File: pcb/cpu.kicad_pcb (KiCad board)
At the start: 2 copper layers, 181.5 x 172.5 mm, 173 parts, among them J1 Conn_01x05, J2 Conn_02x20_Odd_Even, J3 Conn_01x03, SW1 SW_DIP_x03 - Clock Source Sel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, SW2 SW_Push, SW4 SW_Push, U1 LM555, U10 74HCT574, U11 74HC245, U112 74LS574, U113 SST39SF040, U114 74HC04, U117 74LS08, U119 74LS32, U12 74HCT574, U120 74LS32, U121 74HCT574, U122 74HC245, U13 74LS273, U14 74HCT574, U15 74LS273, U16 74HCT574, U17 74HC238, U18 74HCT574, U19 74HC238, U2 74HC14, U20 74HC238, U21 74HCT574, U22 74HCT574, U23 74LS139, U24 28C256, U25 HDSP-7803, U26 HDSP-7803, U27 HDSP-7803, U28 HDSP-7803, U29 74HCT574, U3 74151, U30 74HC86, U31 SST39SF040, U32 74HCT574, U33 74LS08, U34 74HCT574, U35 74LS107, U36 74HC238, U37 74LS138, U38 74HC74, U39 74HC590, U4 LM555 - Button Clock, U40 74HCT574, U41 74LS138, U49 74HCT574, U5 74HC04, U50 74HCT574, U6 74HC590, U7 74HC245, U71 SST39SF040, U72 628128, U8 74HCT574, U80 74HCT574, U81 74HCT574, U82 74HCT574, U83 74HC245, U84 628128, U85 74LS153, U86 74HC245, U87 74LS574, U88 SST39SF040, U89 74LS574, U9 74HC245, U90 SST39SF040, U95 74LS154, U96 74LS154, Y1 12MHz

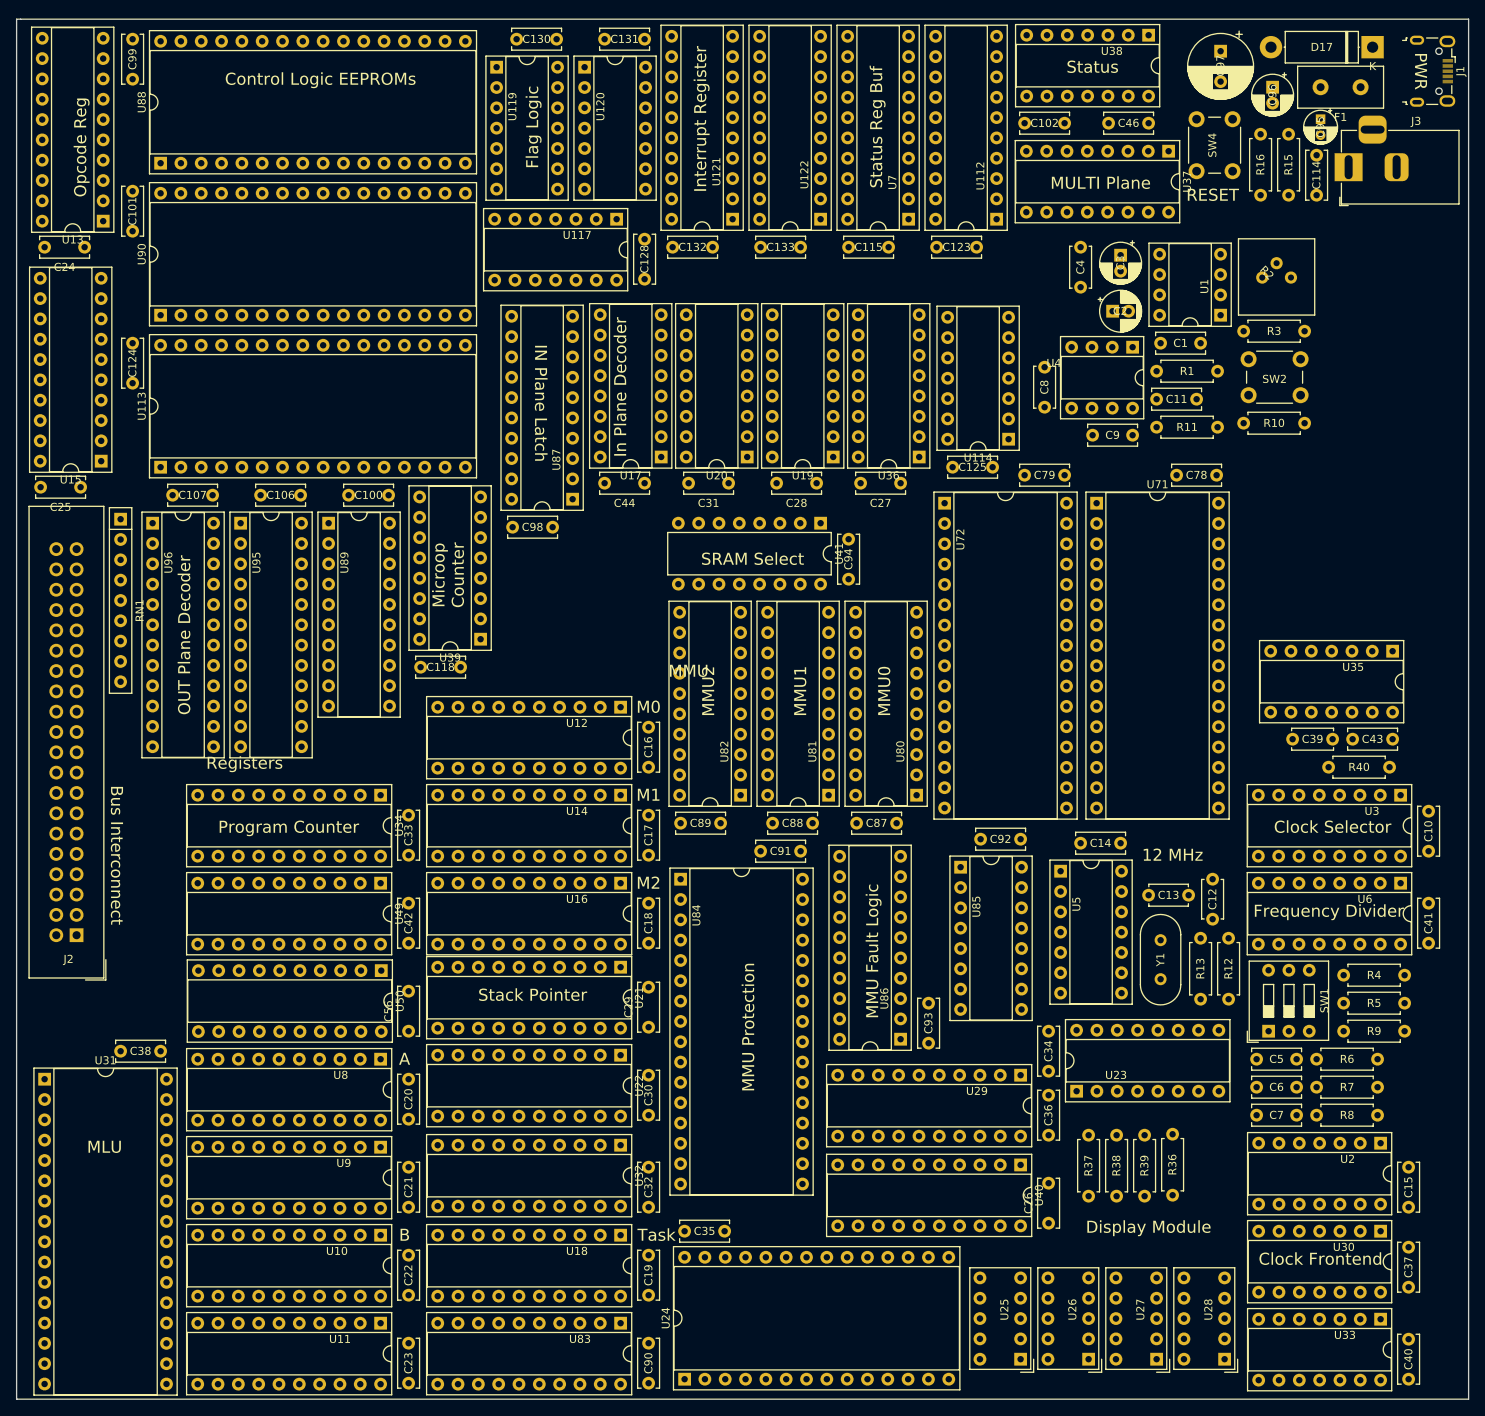
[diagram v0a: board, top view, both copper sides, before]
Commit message: Work on moving everything to 32 bit + proper paging + memory mapped IO.
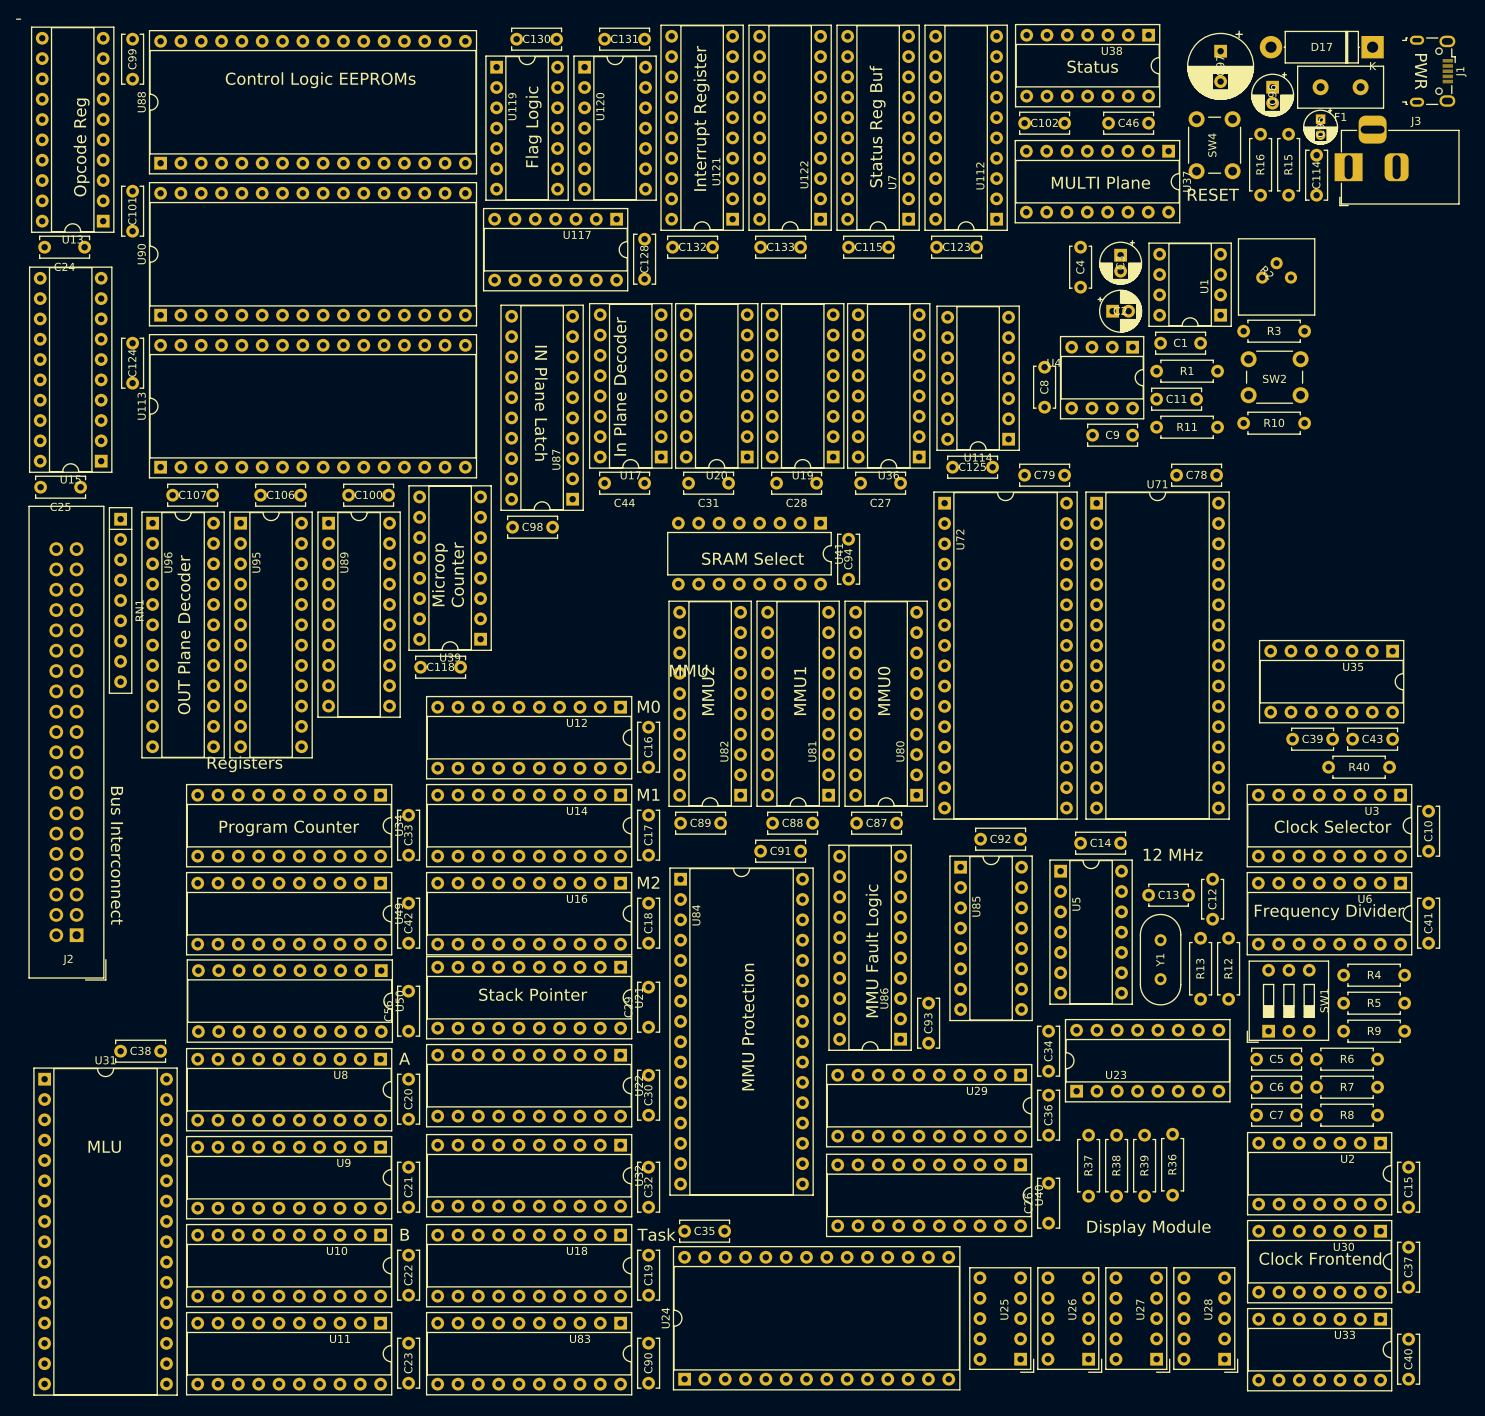
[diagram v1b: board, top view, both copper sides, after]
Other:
- board outline removed
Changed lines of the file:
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@@
-(kicad_pcb (version 20171130) (host pcbnew "(6.0.0-rc1-dev-290-g3eb3db02c)")
+(kicad_pcb (version 20171130) (host pcbnew 5.0.0-fee4fd1~66~ubuntu18.04.1)
   (general
     (thickness 1.6)
-    (drawings 41)
+    (drawings 37)
     (tracks 0)
     (zones 0)
@@
     (zone_45_only no)
     (trace_min 0.2)
+    (segment_width 0.2)
+    (edge_width 0.15)
     (via_size 0.6)
     (via_drill 0.3)
@@
     (uvia_min_size 0.2)
     (uvia_min_drill 0.1)
-    (edge_width 0.15)
-    (segment_width 0.2)
     (pcb_text_width 0.3)
     (pcb_text_size 1.5 1.5)
@@
   )
   (gr_line (start -0.5 0) (end 0 0) (layer Edge.Cuts) (width 0.15))
-  (gr_line (start -0.5 172.5) (end -0.5 0) (layer Edge.Cuts) (width 0.15))
-  (gr_line (start 181 172.5) (end -0.5 172.5) (layer Edge.Cuts) (width 0.15))
-  (gr_line (start 181 0) (end 181 172.5) (layer Edge.Cuts) (width 0.15))
-  (gr_line (start 0 0) (end 181 0) (layer Edge.Cuts) (width 0.15))
   (gr_text "MMU Fault Logic" (at 106.5 116.5 90) (layer F.SilkS)
     (effects (font (size 1.5 1.5) (thickness 0.3)))

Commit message: Conversion to 32-bit word mostly done?
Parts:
- removed C115, C128, C130, C131, C133: 0.1uF, Capacitor_THT:C_Disc_D6.0mm_W2.5mm_P5.00mm
- removed R36, R37, R38, R39: 100, Resistor_THT:R_Axial_DIN0207_L6.3mm_D2.5mm_P7.62mm_Horizontal
- removed U117: 74LS08, Package_DIP:DIP-14_W7.62mm_Socket
- removed U119, U120: 74LS32, Package_DIP:DIP-14_W7.62mm_Socket
- removed U122, U86: 74HC245, Package_DIP:DIP-20_W7.62mm_Socket
- added C45: 0.1uF, Capacitor_THT:C_Disc_D6.0mm_W2.5mm_P5.00mm, F.Cu at (354.9, 39.0)
- added C47: 0.1uF, Capacitor_THT:C_Disc_D6.0mm_W2.5mm_P5.00mm, F.Cu at (354.9, 35.0)
- added C48: 0.1uF, Capacitor_THT:C_Disc_D6.0mm_W2.5mm_P5.00mm, F.Cu at (354.9, 43.1)
- added C49: 0.1uF, Capacitor_THT:C_Disc_D6.0mm_W2.5mm_P5.00mm, F.Cu at (401.9, 7.88)
- added C50: 0.1uF, Capacitor_THT:C_Disc_D6.0mm_W2.5mm_P5.00mm, F.Cu at (410.1, 7.88)
- added C51: 0.1uF, Capacitor_THT:C_Disc_D6.0mm_W2.5mm_P5.00mm, F.Cu at (401.9, 11.9)
- added C52: 0.1uF, Capacitor_THT:C_Disc_D6.0mm_W2.5mm_P5.00mm, F.Cu at (410.1, 11.9)
- added C53: 0.1uF, Capacitor_THT:C_Disc_D6.0mm_W2.5mm_P5.00mm, F.Cu at (401.9, 16.0)
- added C54: 0.1uF, Capacitor_THT:C_Disc_D6.0mm_W2.5mm_P5.00mm, F.Cu at (401.9, 20.0)
- added C55: 0.1uF, Capacitor_THT:C_Disc_D6.0mm_W2.5mm_P5.00mm, F.Cu at (390.2, 27.4)
- added C57: 0.1uF, Capacitor_THT:C_Disc_D6.0mm_W2.5mm_P5.00mm, F.Cu at (406.5, 118.1)
- added C58: 0.1uF, Capacitor_THT:C_Disc_D6.0mm_W2.5mm_P5.00mm, F.Cu at (398.3, 118.1)
- added C59: 0.1uF, Capacitor_THT:C_Disc_D6.0mm_W2.5mm_P5.00mm, F.Cu at (410.1, 89.7)
- added C60: 0.1uF, Capacitor_THT:C_Disc_D6.0mm_W2.5mm_P5.00mm, F.Cu at (418.2, 85.6)
- added C61: 0.1uF, Capacitor_THT:C_Disc_D6.0mm_W2.5mm_P5.00mm, F.Cu at (410.1, 85.6)
- added C62: 0.1uF, Capacitor_THT:C_Disc_D6.0mm_W2.5mm_P5.00mm, F.Cu at (362.9, 76.8)
- added C63: 0.1uF, Capacitor_THT:C_Disc_D6.0mm_W2.5mm_P5.00mm, F.Cu at (354.7, 76.8)
- added C64: 0.1uF, Capacitor_THT:C_Disc_D6.0mm_W2.5mm_P5.00mm, F.Cu at (354.7, 80.9)
- added C65: 0.1uF, Capacitor_THT:C_Disc_D6.0mm_W2.5mm_P5.00mm, F.Cu at (468.4, 7.88)
- added C66: 0.1uF, Capacitor_THT:C_Disc_D6.0mm_W2.5mm_P5.00mm, F.Cu at (476.5, 7.88)
- added C67: 0.1uF, Capacitor_THT:C_Disc_D6.0mm_W2.5mm_P5.00mm, F.Cu at (468.4, 11.9)
- added C68: 0.1uF, Capacitor_THT:C_Disc_D6.0mm_W2.5mm_P5.00mm, F.Cu at (362.9, 109.3)
- added C69: 0.1uF, Capacitor_THT:C_Disc_D6.0mm_W2.5mm_P5.00mm, F.Cu at (354.7, 113.4)
- added C70: 0.1uF, Capacitor_THT:C_Disc_D6.0mm_W2.5mm_P5.00mm, F.Cu at (354.7, 109.3)
- added C71: 0.1uF, Capacitor_THT:C_Disc_D6.0mm_W2.5mm_P5.00mm, F.Cu at (410.1, 53.2)
- added C72: 0.1uF, Capacitor_THT:C_Disc_D6.0mm_W2.5mm_P5.00mm, F.Cu at (418.2, 53.2)
- added C73: 0.1uF, Capacitor_THT:C_Disc_D6.0mm_W2.5mm_P5.00mm, F.Cu at (410.1, 57.2)
- added C74: 0.1uF, Capacitor_THT:C_Disc_D6.0mm_W2.5mm_P5.00mm, F.Cu at (234.8, 152.9)
- added C75: 0.1uF, Capacitor_THT:C_Disc_D6.0mm_W2.5mm_P5.00mm, F.Cu at (242.9, 152.9)
- added C76: 0.1uF, Capacitor_THT:C_Disc_D6.0mm_W2.5mm_P5.00mm, F.Cu at (251.1, 152.9)
- added C77: 0.1uF, Capacitor_THT:C_Disc_D6.0mm_W2.5mm_P5.00mm, F.Cu at (259.2, 152.9)
- added C80: 0.1uF, Capacitor_THT:C_Disc_D6.0mm_W2.5mm_P5.00mm, F.Cu at (293.0, 80.9)
- added C81: 0.1uF, Capacitor_THT:C_Disc_D6.0mm_W2.5mm_P5.00mm, F.Cu at (301.1, 76.8)
- added C82: 0.1uF, Capacitor_THT:C_Disc_D6.0mm_W2.5mm_P5.00mm, F.Cu at (293.0, 76.8)
- added C83: 0.1uF, Capacitor_THT:C_Disc_D6.0mm_W2.5mm_P5.00mm, F.Cu at (281.8, 145.3)
- added C84: 0.1uF, Capacitor_THT:C_Disc_D6.0mm_W2.5mm_P5.00mm, F.Cu at (468.4, 44.4)
- added C85: 0.1uF, Capacitor_THT:C_Disc_D6.0mm_W2.5mm_P5.00mm, F.Cu at (468.4, 40.3)
- added C86: 0.1uF, Capacitor_THT:C_Disc_D6.0mm_W2.5mm_P5.00mm, F.Cu at (476.5, 40.3)
- added D1: D, Diode_THT:D_DO-41_SOD81_P7.62mm_Horizontal, F.Cu at (304.8, 205.7)
- added D10: D, Diode_THT:D_DO-41_SOD81_P7.62mm_Horizontal, F.Cu at (304.8, 197.2)
- added D11: D, Diode_THT:D_DO-41_SOD81_P7.62mm_Horizontal, F.Cu at (282.0, 210.0)
- added D12: D, Diode_THT:D_DO-41_SOD81_P7.62mm_Horizontal, F.Cu at (293.4, 201.5)
- added D13: D, Diode_THT:D_DO-41_SOD81_P7.62mm_Horizontal, F.Cu at (282.0, 205.7)
- added D14: D, Diode_THT:D_DO-41_SOD81_P7.62mm_Horizontal, F.Cu at (293.4, 197.2)
- added D15: D, Diode_THT:D_DO-41_SOD81_P7.62mm_Horizontal, F.Cu at (282.0, 197.2)
- added D16: D, Diode_THT:D_DO-41_SOD81_P7.62mm_Horizontal, F.Cu at (316.2, 222.7)
- added D18: D, Diode_THT:D_DO-41_SOD81_P7.62mm_Horizontal, F.Cu at (282.0, 201.5)
- added D19: D, Diode_THT:D_DO-41_SOD81_P7.62mm_Horizontal, F.Cu at (327.5, 210.0)
- added D2: D, Diode_THT:D_DO-41_SOD81_P7.62mm_Horizontal, F.Cu at (293.4, 214.2)
- added D20: D, Diode_THT:D_DO-41_SOD81_P7.62mm_Horizontal, F.Cu at (327.5, 205.7)
- added D21: D, Diode_THT:D_DO-41_SOD81_P7.62mm_Horizontal, F.Cu at (316.2, 218.5)
- added D22: D, Diode_THT:D_DO-41_SOD81_P7.62mm_Horizontal, F.Cu at (316.2, 214.2)
- added D23: D, Diode_THT:D_DO-41_SOD81_P7.62mm_Horizontal, F.Cu at (304.8, 222.7)
- added D24: D, Diode_THT:D_DO-41_SOD81_P7.62mm_Horizontal, F.Cu at (304.8, 218.5)
- added D25: D, Diode_THT:D_DO-41_SOD81_P7.62mm_Horizontal, F.Cu at (316.2, 210.0)
- added D26: D, Diode_THT:D_DO-41_SOD81_P7.62mm_Horizontal, F.Cu at (316.2, 201.5)
- added D27: D, Diode_THT:D_DO-41_SOD81_P7.62mm_Horizontal, F.Cu at (327.5, 201.5)
- added D28: D, Diode_THT:D_DO-41_SOD81_P7.62mm_Horizontal, F.Cu at (316.2, 205.7)
- added D29: D, Diode_THT:D_DO-41_SOD81_P7.62mm_Horizontal, F.Cu at (304.8, 214.2)
- added D3: D, Diode_THT:D_DO-41_SOD81_P7.62mm_Horizontal, F.Cu at (316.2, 197.2)
- added D30: D, Diode_THT:D_DO-41_SOD81_P7.62mm_Horizontal, F.Cu at (327.5, 197.2)
- added D31: D, Diode_THT:D_DO-41_SOD81_P7.62mm_Horizontal, F.Cu at (293.4, 222.7)
- added D32: D, Diode_THT:D_DO-41_SOD81_P7.62mm_Horizontal, F.Cu at (293.4, 218.5)
- added D33: D, Diode_THT:D_DO-41_SOD81_P7.62mm_Horizontal, F.Cu at (304.8, 210.0)
- added D4: D, Diode_THT:D_DO-41_SOD81_P7.62mm_Horizontal, F.Cu at (282.0, 222.7)
- added D5: D, Diode_THT:D_DO-41_SOD81_P7.62mm_Horizontal, F.Cu at (282.0, 218.5)
- added D6: D, Diode_THT:D_DO-41_SOD81_P7.62mm_Horizontal, F.Cu at (293.4, 210.0)
- added D7: D, Diode_THT:D_DO-41_SOD81_P7.62mm_Horizontal, F.Cu at (304.8, 201.5)
- added D8: D, Diode_THT:D_DO-41_SOD81_P7.62mm_Horizontal, F.Cu at (293.4, 205.7)
- added D9: D, Diode_THT:D_DO-41_SOD81_P7.62mm_Horizontal, F.Cu at (282.0, 214.2)
- added J4: Conn_02x20_Odd_Even, Connector_IDC:IDC-Header_2x20_P2.54mm_Vertical, F.Cu at (237.4, 12.0)
- added U42: 74HC245, Package_DIP:DIP-20_W7.62mm_Socket, F.Cu at (355.4, 7.98)
- added U43: 74HC00, Package_DIP:DIP-14_W7.62mm_Socket, F.Cu at (378.9, 27.5)
- added U44: 74HC00, Package_DIP:DIP-14_W7.62mm_Socket, F.Cu at (367.2, 27.5)
- added U45: 74HC00, Package_DIP:DIP-14_W7.62mm_Socket, F.Cu at (378.9, 7.98)
- added U46: 74HC00, Package_DIP:DIP-14_W7.62mm_Socket, F.Cu at (367.2, 7.98)
- added U47: 74HC00, Package_DIP:DIP-14_W7.62mm_Socket, F.Cu at (390.7, 7.98)
- added U48: 74HCT574, Package_DIP:DIP-20_W7.62mm_Socket, F.Cu at (375.3, 118.2)
- added U51: 74HCT574, Package_DIP:DIP-20_W7.62mm_Socket, F.Cu at (398.8, 85.7)
- added U52: 74HCT574, Package_DIP:DIP-20_W7.62mm_Socket, F.Cu at (387.1, 85.7)
- added U53: 74HCT574, Package_DIP:DIP-20_W7.62mm_Socket, F.Cu at (375.3, 85.7)
- added U54: 74HCT574, Package_DIP:DIP-20_W7.62mm_Socket, F.Cu at (320.0, 76.9)
- added U55: 74HCT574, Package_DIP:DIP-20_W7.62mm_Socket, F.Cu at (331.7, 76.9)
- added U56: 74HCT574, Package_DIP:DIP-20_W7.62mm_Socket, F.Cu at (343.5, 76.9)
- added U57: 74HCT574, Package_DIP:DIP-20_W7.62mm_Socket, F.Cu at (433.6, 7.98)
- added U58: 74HCT574, Package_DIP:DIP-20_W7.62mm_Socket, F.Cu at (457.1, 7.98)
- added U59: 74HCT574, Package_DIP:DIP-20_W7.62mm_Socket, F.Cu at (445.4, 7.98)
- added U60: 74HCT574, Package_DIP:DIP-20_W7.62mm_Socket, F.Cu at (343.5, 109.4)
- added U61: 74HCT574, Package_DIP:DIP-20_W7.62mm_Socket, F.Cu at (320.0, 109.4)
- added U62: 74HCT574, Package_DIP:DIP-20_W7.62mm_Socket, F.Cu at (331.7, 109.4)
- added U63: 74HCT574, Package_DIP:DIP-20_W7.62mm_Socket, F.Cu at (387.1, 53.3)
- added U64: 74HCT574, Package_DIP:DIP-20_W7.62mm_Socket, F.Cu at (375.3, 53.3)
- added U65: 74HCT574, Package_DIP:DIP-20_W7.62mm_Socket, F.Cu at (398.8, 53.3)
- added U66: 74LS32, Package_DIP:DIP-14_W7.62mm_Socket, F.Cu at (282.3, 125.9)
- added U67: 74HCT574, Package_DIP:DIP-20_W7.62mm_Socket, F.Cu at (247.0, 125.9)
- added U68: 74HCT574, Package_DIP:DIP-20_W7.62mm_Socket, F.Cu at (258.8, 125.9)
- added U69: 74HCT574, Package_DIP:DIP-20_W7.62mm_Socket, F.Cu at (235.3, 125.9)
- added U70: 74HCT574, Package_DIP:DIP-20_W7.62mm_Socket, F.Cu at (270.5, 125.9)
- added U73: 628128, Package_DIP:DIP-32_W15.24mm_Socket, F.Cu at (235.3, 76.9)
- added U74: 628128, Package_DIP:DIP-32_W15.24mm_Socket, F.Cu at (274.1, 76.9)
- added U75: 628128, Package_DIP:DIP-32_W15.24mm_Socket, F.Cu at (254.7, 76.9)
- added U76: 74HCT574, Package_DIP:DIP-20_W7.62mm_Socket, F.Cu at (433.6, 40.4)
- added U77: 74HCT574, Package_DIP:DIP-20_W7.62mm_Socket, F.Cu at (445.4, 40.4)
- added U78: 74HCT574, Package_DIP:DIP-20_W7.62mm_Socket, F.Cu at (457.1, 40.4)
- added U79: 74HCT574, Package_DIP:DIP-20_W7.62mm_Socket, F.Cu at (387.1, 118.2)
- U11: value 74HC245 -> 74LS283; footprint Package_DIP:DIP-20_W7.62mm_Socket -> Package_DIP:DIP-16_W7.62mm_Socket
- U14, U22, U34, U40: value 74HCT574 -> 74LS283; footprint Package_DIP:DIP-20_W7.62mm_Socket -> Package_DIP:DIP-16_W7.62mm_Socket
- U16, U18, U29: value 74HCT574 -> 74HC245
- U21, U32: value 74HCT574 -> 74HC00; footprint Package_DIP:DIP-20_W7.62mm_Socket -> Package_DIP:DIP-14_W7.62mm_Socket
- U23: value 74LS139 -> 74LS283
- U24: value 28C256 -> 74HC245; footprint Package_DIP:DIP-28_W15.24mm_Socket -> Package_DIP:DIP-20_W7.62mm_Socket
- U25: value HDSP-7803 -> 74HC245; footprint Display_7Segment:HDSP-7801 -> Package_DIP:DIP-20_W7.62mm_Socket
- U26: value HDSP-7803 -> 74HC00; footprint Display_7Segment:HDSP-7801 -> Package_DIP:DIP-14_W7.62mm_Socket
- U27, U28: value HDSP-7803 -> 74LS283; footprint Display_7Segment:HDSP-7801 -> Package_DIP:DIP-16_W7.62mm_Socket
- U31: value SST39SF040 -> 74HC245; footprint Package_DIP:DIP-32_W15.24mm_Socket -> Package_DIP:DIP-20_W7.62mm_Socket
- U38: value 74HC74 -> 74LS574; footprint Package_DIP:DIP-14_W7.62mm_Socket -> Package_DIP:DIP-20_W7.62mm_Socket
- U41: value 74LS138 -> 74HC245; footprint Package_DIP:DIP-16_W7.62mm -> Package_DIP:DIP-20_W7.62mm_Socket
- U7: value 74HC245 -> 74LS574
- U83, U9: value 74HC245 -> 74HCT574
- U84: value 628128 -> 74LS574; footprint Package_DIP:DIP-32_W15.24mm_Socket -> Package_DIP:DIP-20_W7.62mm_Socket
- U85: value 74LS153 -> 74HCT574; footprint Package_DIP:DIP-16_W7.62mm_Socket -> Package_DIP:DIP-20_W7.62mm_Socket
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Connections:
- C35 pad 1: GND -> VCC
- C35 pad 2: VCC -> GND
- C38 pad 1: GND -> VCC
- C38 pad 2: VCC -> GND
- C91 pad 1: GND -> VCC
- C91 pad 2: VCC -> GND
- C92 pad 1: VCC -> GND
- C92 pad 2: GND -> VCC
- C93 pad 1: VCC -> GND
- C93 pad 2: GND -> VCC
- J1 pad 2: (no net) -> Net-(J1-Pad2)
- J1 pad 3: (no net) -> Net-(J1-Pad3)
- J1 pad 4: (no net) -> Net-(J1-Pad4)
- J2 pad 10: /INT0_IN_CLK -> /BUS10
- J2 pad 11: /BUS1 -> /~MMU_OUT_NCLK
- J2 pad 12: /INT1_IN_CLK -> /BUS11
- J2 pad 13: /BUS2 -> /INT0
- J2 pad 14: /INT2_IN_CLK -> /BUS12
- J2 pad 15: /BUS3 -> /INT1
- J2 pad 16: /INT3_IN_CLK -> /BUS13
- J2 pad 17: /BUS4 -> /INT2
- J2 pad 18: /INT4_IN_CLK -> /BUS14
- J2 pad 19: /BUS5 -> /INT3
- J2 pad 2: VCC -> /BUS6
- J2 pad 20: /INT5_IN_CLK -> /BUS15
- J2 pad 21: /BUS6 -> /INT4
- J2 pad 22: /INT6_IN_CLK -> /BUS16
- J2 pad 23: /BUS7 -> /INT5
- J2 pad 24: /INT7_IN_CLK -> /BUS17
- J2 pad 25: /INT0 -> /INT6
- J2 pad 26: /~INT0_OUT_NCLK -> /BUS18
- J2 pad 27: /INT1 -> /INT7
- J2 pad 28: /~INT1_OUT_NCLK -> /BUS19
- J2 pad 29: /INT2 -> /BUS0
- J2 pad 3: VCC -> GND
- J2 pad 30: /~INT2_OUT_NCLK -> /BUS20
- J2 pad 31: /INT3 -> /BUS1
- J2 pad 32: /~INT3_OUT_NCLK -> /BUS21
- J2 pad 33: /INT4 -> /BUS2
- J2 pad 34: /~INT4_OUT_NCLK -> /BUS22
- J2 pad 35: /INT5 -> /BUS3
- J2 pad 36: /~INT5_OUT_NCLK -> /BUS23
- J2 pad 37: /INT6 -> /BUS4
- J2 pad 38: /~INT6_OUT_NCLK -> /BUS24
- J2 pad 39: /INT7 -> /BUS5
- J2 pad 4: GND -> /BUS7
- J2 pad 40: /~INT7_OUT_NCLK -> /BUS25
- J2 pad 6: GND -> /BUS8
- J2 pad 8: GND -> /BUS9
- J2 pad 9: /BUS0 -> /~MMU_IN_CLK
- J3 pad 3: (no net) -> Net-(J3-Pad3)
- U10 pad 11: /B_IN_CLK -> /ADDR_IN_CLK
- U10 pad 12: /B7 -> /ADDR23
- U10 pad 13: /B6 -> /ADDR22
- U10 pad 14: /B5 -> /ADDR21
- U10 pad 15: /B4 -> /ADDR20
- U10 pad 16: /B3 -> /ADDR19
- U10 pad 17: /B2 -> /ADDR18
- U10 pad 18: /B1 -> /ADDR17
- U10 pad 19: /B0 -> /ADDR16
- U10 pad 2: /BUS0 -> /BUS16
- U10 pad 3: /BUS1 -> /BUS17
- U10 pad 4: /BUS2 -> /BUS18
- U10 pad 5: /BUS3 -> /BUS19
- U10 pad 6: /BUS4 -> /BUS20
- U10 pad 7: /BUS5 -> /BUS21
- U10 pad 8: /BUS6 -> /BUS22
- U10 pad 9: /BUS7 -> /BUS23
- U11 pad 1: VCC -> /ALU/SUM1
- U11 pad 10: GND -> /ALU/SUM3
- U11 pad 11: /BUS7 -> /ALU/B3
- U11 pad 12: /BUS6 -> /ALU/A3
- U11 pad 13: /BUS5 -> /ALU/SUM2
- U11 pad 14: /BUS4 -> /ALU/A2
- U11 pad 15: /BUS3 -> /ALU/B2
- U11 pad 16: /BUS2 -> VCC
- U11 pad 2: /B0 -> /ALU/B1
- U11 pad 3: /B1 -> /ALU/A1
- U11 pad 4: /B2 -> /ALU/SUM0
- U11 pad 5: /B3 -> /ALU/A0
- U11 pad 6: /B4 -> /ALU/B0
- U11 pad 7: /B5 -> /CARRY_IN
- U11 pad 8: /B6 -> GND
- U11 pad 9: /B7 -> /ALU/CARRY0
- U112 pad 1: /Control Logic/~CTRLLOGIC_OUT_NCLK -> /Control Logic/~BUS0_OUT_NCLK
- U113 pad 1: /Control Logic/MMU_FAULT_FLAG -> /Control Logic/MICROOP4
- U113 pad 2: /Control Logic/MICROOP4 -> /Control Logic/MICROOP2
- U113 pad 28: /Control Logic/MICROOP1 -> /Control Logic/OP13
- U113 pad 29: /Control Logic/MICROOP2 -> /Control Logic/MICROOP0
- U113 pad 3: /Control Logic/MICROOP3 -> /Control Logic/MICROOP1
- U113 pad 30: /Control Logic/INT_FLAG -> /Control Logic/MICROOP3
- U113 pad 4: /Control Logic/MICROOP0 -> /Control Logic/OP12
- U114 pad 13: /MMU/M20 -> GND
- U114 pad 3: /Control Logic/MMU_CONTROL_IN_CLK -> GND
- U114 pad 4: /~MMU_CONTROL_IN_CLK -> Net-(U114-Pad4)
- U114 pad 6: (no net) -> Net-(U114-Pad6)
- U12 pad 1: /~M0_OUT_NCLK -> /~A_OUT_NCLK
- U12 pad 11: /M0_IN_CLK -> /A_IN_CLK
- U121 pad 1: GND -> /~INT_OUT_NCLK
- U121 pad 12: /INT7_LATCH -> /BUS7
- U121 pad 13: /INT6_LATCH -> /BUS6
- U121 pad 14: /INT5_LATCH -> /BUS5
- U121 pad 15: /INT4_LATCH -> /BUS4
- U121 pad 16: /INT3_LATCH -> /BUS3
- U121 pad 17: /INT2_LATCH -> /BUS2
- U121 pad 18: /INT1_LATCH -> /BUS1
- U121 pad 19: /INT0_LATCH -> /BUS0
- U14 pad 1: /~M1_OUT_NCLK -> /ALU/SUM5
- U14 pad 10: GND -> /ALU/SUM7
- U14 pad 11: /M1_IN_CLK -> /ALU/B7
- U14 pad 12: /BUS7 -> /ALU/A7
- U14 pad 13: /BUS6 -> /ALU/SUM6
- U14 pad 14: /BUS5 -> /ALU/A6
- U14 pad 15: /BUS4 -> /ALU/B6
- U14 pad 16: /BUS3 -> VCC
- U14 pad 2: /BUS0 -> /ALU/B5
- U14 pad 3: /BUS1 -> /ALU/A5
- U14 pad 4: /BUS2 -> /ALU/SUM4
- U14 pad 5: /BUS3 -> /ALU/A4
- U14 pad 6: /BUS4 -> /ALU/B4
- U14 pad 7: /BUS5 -> /ALU/CARRY0
- U14 pad 8: /BUS6 -> GND
- U14 pad 9: /BUS7 -> /ALU/CARRY1
- U15 pad 12: (no net) -> /Control Logic/OP12
- U15 pad 15: (no net) -> /Control Logic/OP13
- U15 pad 16: (no net) -> Net-(U15-Pad16)
- U15 pad 19: (no net) -> Net-(U15-Pad19)
- U16 pad 1: /~M2_OUT_NCLK -> VCC
- U16 pad 11: /M2_IN_CLK -> /BUS7
- U16 pad 12: /BUS7 -> /BUS6
- U16 pad 13: /BUS6 -> /BUS5
- U16 pad 14: /BUS5 -> /BUS4
- U16 pad 15: /BUS4 -> /BUS3
- U16 pad 16: /BUS3 -> /BUS2
- U16 pad 17: /BUS2 -> /BUS1
- U16 pad 18: /BUS1 -> /BUS0
- U16 pad 19: /BUS0 -> /~SUM_OUT_NCLK
- U16 pad 2: /BUS0 -> /ALU/SUM0
- U16 pad 3: /BUS1 -> /ALU/SUM1
- U16 pad 4: /BUS2 -> /ALU/SUM2
- U16 pad 5: /BUS3 -> /ALU/SUM3
- U16 pad 6: /BUS4 -> /ALU/SUM4
- U16 pad 7: /BUS5 -> /ALU/SUM5
- U16 pad 8: /BUS6 -> /ALU/SUM6
- U16 pad 9: /BUS7 -> /ALU/SUM7
- U17 pad 10: /M2_IN_CLK -> /ALU0_IN_CLK
- U17 pad 11: /M1_IN_CLK -> /PC_IN_CLK
- U17 pad 12: /M0_IN_CLK -> /SP_IN_CLK
- U17 pad 15: (no net) -> /Control Logic/IN decoder/O0
- U17 pad 7: /S1_IN_CLK -> /ADDR_IN_CLK
- U17 pad 9: /S0_IN_CLK -> /ALU1_IN_CLK
- U18 pad 1: GND -> VCC
- U18 pad 11: /TASK_IN_CLK -> /BUS7
- U18 pad 12: /TASK7 -> /BUS6
- U18 pad 13: /TASK6 -> /BUS5
- U18 pad 14: /TASK5 -> /BUS4
- U18 pad 15: /TASK4 -> /BUS3
- U18 pad 16: /TASK3 -> /BUS2
- U18 pad 17: /TASK2 -> /BUS1
- U18 pad 18: /TASK1 -> /BUS0
- U18 pad 19: /TASK0 -> /~NAND_OUT_NCLK
- U18 pad 2: /BUS0 -> /ALU/NAND0
- U18 pad 3: /BUS1 -> /ALU/NAND1
- U18 pad 4: /BUS2 -> /ALU/NAND2
- U18 pad 5: /BUS3 -> /ALU/NAND3
- U18 pad 6: /BUS4 -> /ALU/NAND4
- U18 pad 7: /BUS5 -> /ALU/NAND5
- U18 pad 8: /BUS6 -> /ALU/NAND6
- U18 pad 9: /BUS7 -> /ALU/NAND7
- U19 pad 10: /MMU1_IN_CLK -> /M3_IN_CLK
- U19 pad 11: /MMU0_IN_CLK -> /M2_IN_CLK
- U19 pad 12: /PC2_IN_CLK -> /M1_IN_CLK
- U19 pad 13: /PC1_IN_CLK -> /M0_IN_CLK
- U19 pad 14: /PC0_IN_CLK -> /M_IN_CLK
- U19 pad 15: /S2_IN_CLK -> /Control Logic/MMU_IN_CLK
- U19 pad 7: /Control Logic/MMU_IN_CLK -> /STATUS_IN_CLK
- U19 pad 9: /MMU2_IN_CLK -> /PAGE_IN_CLK
- U2 pad 8: (no net) -> Net-(U2-Pad8)
- U20 pad 10: /Control Logic/OPCODE1_IN_CLK -> /Control Logic/IN decoder/O21
- U20 pad 11: /Control Logic/OPCODE0_IN_CLK -> /Control Logic/IN decoder/O20
- U20 pad 12: /TASK_IN_CLK -> /Control Logic/IN decoder/O19
- U20 pad 13: /DISP_MODE_IN_CLK -> /Control Logic/OPCODE1_IN_CLK
- U20 pad 14: /DISP_IN_CLK -> /Control Logic/OPCODE0_IN_CLK
- U20 pad 15: /Control Logic/MMU_CONTROL_IN_CLK -> /INT_IN_CLK
- U20 pad 7: (no net) -> /Control Logic/IN decoder/O23
- U20 pad 9: /INT_IN_CLK -> /Control Logic/IN decoder/O22
- U21 pad 1: /~S0_OUT_NCLK -> /ALU/A0
- U21 pad 10: GND -> /ALU/B2
- U21 pad 11: /S0_IN_CLK -> /ALU/NAND3
- U21 pad 12: /BUS7 -> /ALU/A3
- U21 pad 13: /BUS6 -> /ALU/B3
- U21 pad 14: /BUS5 -> VCC
- U21 pad 2: /BUS0 -> /ALU/B0
- U21 pad 3: /BUS1 -> /ALU/NAND0
- U21 pad 4: /BUS2 -> /ALU/A1
- U21 pad 5: /BUS3 -> /ALU/B1
- U21 pad 6: /BUS4 -> /ALU/NAND1
- U21 pad 7: /BUS5 -> GND
- U21 pad 8: /BUS6 -> /ALU/NAND2
- U21 pad 9: /BUS7 -> /ALU/A2
- U22 pad 1: /~S1_OUT_NCLK -> /ALU/SUM9
- U22 pad 10: GND -> /ALU/SUM11
- U22 pad 11: /S1_IN_CLK -> /ALU/B11
- U22 pad 12: /BUS7 -> /ALU/A11
- U22 pad 13: /BUS6 -> /ALU/SUM10
- U22 pad 14: /BUS5 -> /ALU/A10
- U22 pad 15: /BUS4 -> /ALU/B10
- U22 pad 16: /BUS3 -> VCC
- U22 pad 2: /BUS0 -> /ALU/B9
- U22 pad 3: /BUS1 -> /ALU/A9
- U22 pad 4: /BUS2 -> /ALU/SUM8
- U22 pad 5: /BUS3 -> /ALU/A8
- U22 pad 6: /BUS4 -> /ALU/B8
- U22 pad 7: /BUS5 -> /ALU/CARRY1
- U22 pad 8: /BUS6 -> GND
- U22 pad 9: /BUS7 -> /ALU/CARRY2
- U23 pad 1: GND -> /ALU/SUM13
- U23 pad 10: (no net) -> /ALU/SUM15
- U23 pad 11: (no net) -> /ALU/B15
- U23 pad 12: (no net) -> /ALU/A15
- U23 pad 13: (no net) -> /ALU/SUM14
- U23 pad 14: (no net) -> /ALU/A14
- U23 pad 15: (no net) -> /ALU/B14
- U23 pad 2: /47KHZ_CLK -> /ALU/B13
- U23 pad 3: /94KHZ_CLK -> /ALU/A13
- U23 pad 4: Net-(R36-Pad2) -> /ALU/SUM12
- U23 pad 5: Net-(R37-Pad2) -> /ALU/A12
- U23 pad 6: Net-(R38-Pad2) -> /ALU/B12
- U23 pad 7: Net-(R39-Pad2) -> /ALU/CARRY2
- U23 pad 9: (no net) -> /ALU/CARRY3
- U24 pad 1: /94KHZ_CLK -> VCC
- U24 pad 10: /Display/Display Register/O0 -> GND
- U24 pad 11: /Display/O0 -> /BUS15
- U24 pad 12: /Display/O1 -> /BUS14
- U24 pad 13: /Display/O2 -> /BUS13
- U24 pad 14: GND -> /BUS12
- U24 pad 15: /Display/O3 -> /BUS11
- U24 pad 16: /Display/O4 -> /BUS10
- U24 pad 17: /Display/O5 -> /BUS9
- U24 pad 18: /Display/O6 -> /BUS8
- U24 pad 19: /Display/O7 -> /~SUM_OUT_NCLK
- U24 pad 2: /Display/MODE4 -> /ALU/SUM8
- U24 pad 20: GND -> VCC
- U24 pad 3: /Display/Display Register/O7 -> /ALU/SUM9
- U24 pad 4: /Display/Display Register/O6 -> /ALU/SUM10
- U24 pad 5: /Display/Display Register/O5 -> /ALU/SUM11
- U24 pad 6: /Display/Display Register/O4 -> /ALU/SUM12
- U24 pad 7: /Display/Display Register/O3 -> /ALU/SUM13
- U24 pad 8: /Display/Display Register/O2 -> /ALU/SUM14
- U24 pad 9: /Display/Display Register/O1 -> /ALU/SUM15
- U25 pad 1: /Display/L0 -> VCC
- U25 pad 10: /Display/O0 -> GND
- U25 pad 2: /Display/O5 -> /ALU/NAND8
- U25 pad 3: /Display/O6 -> /ALU/NAND9
- U25 pad 4: /Display/O4 -> /ALU/NAND10
- U25 pad 5: /Display/O3 -> /ALU/NAND11
- U25 pad 6: /Display/L0 -> /ALU/NAND12
- U25 pad 7: /Display/O7 -> /ALU/NAND13
- U25 pad 8: /Display/O2 -> /ALU/NAND14
- U25 pad 9: /Display/O1 -> /ALU/NAND15
- U26 pad 1: /Display/L1 -> /ALU/A4
- U26 pad 10: /Display/O0 -> /ALU/B6
- U26 pad 2: /Display/O5 -> /ALU/B4
- U26 pad 3: /Display/O6 -> /ALU/NAND4
- U26 pad 4: /Display/O4 -> /ALU/A5
- U26 pad 5: /Display/O3 -> /ALU/B5
- U26 pad 6: /Display/L1 -> /ALU/NAND5
- U26 pad 7: /Display/O7 -> GND
- U26 pad 8: /Display/O2 -> /ALU/NAND6
- U26 pad 9: /Display/O1 -> /ALU/A6
- U27 pad 1: /Display/L2 -> /ALU/SUM17
- U27 pad 10: /Display/O0 -> /ALU/SUM19
- U27 pad 2: /Display/O5 -> /ALU/B17
- U27 pad 3: /Display/O6 -> /ALU/A17
- U27 pad 4: /Display/O4 -> /ALU/SUM16
- U27 pad 5: /Display/O3 -> /ALU/A16
- U27 pad 6: /Display/L2 -> /ALU/B16
- U27 pad 7: /Display/O7 -> /ALU/CARRY3
- U27 pad 8: /Display/O2 -> GND
- U27 pad 9: /Display/O1 -> /ALU/CARRY4
- U28 pad 1: /Display/L3 -> /ALU/SUM21
- U28 pad 10: /Display/O0 -> /ALU/SUM23
- U28 pad 2: /Display/O5 -> /ALU/B21
- U28 pad 3: /Display/O6 -> /ALU/A21
- U28 pad 4: /Display/O4 -> /ALU/SUM20
- U28 pad 5: /Display/O3 -> /ALU/A20
- U28 pad 6: /Display/L3 -> /ALU/B20
- U28 pad 7: /Display/O7 -> /ALU/CARRY4
- U28 pad 8: /Display/O2 -> GND
- U28 pad 9: /Display/O1 -> /ALU/CARRY5
- U29 pad 1: GND -> VCC
- U29 pad 11: /DISP_IN_CLK -> /BUS23
- U29 pad 12: /Display/Display Register/O7 -> /BUS22
- U29 pad 13: /Display/Display Register/O6 -> /BUS21
- U29 pad 14: /Display/Display Register/O5 -> /BUS20
- U29 pad 15: /Display/Display Register/O4 -> /BUS19
- U29 pad 16: /Display/Display Register/O3 -> /BUS18
- U29 pad 17: /Display/Display Register/O2 -> /BUS17
- U29 pad 18: /Display/Display Register/O1 -> /BUS16
- U29 pad 19: /Display/Display Register/O0 -> /~SUM_OUT_NCLK
- U29 pad 2: /BUS0 -> /ALU/SUM16
- U29 pad 3: /BUS1 -> /ALU/SUM17
- U29 pad 4: /BUS2 -> /ALU/SUM18
- U29 pad 5: /BUS3 -> /ALU/SUM19
- U29 pad 6: /BUS4 -> /ALU/SUM20
- U29 pad 7: /BUS5 -> /ALU/SUM21
- U29 pad 8: /BUS6 -> /ALU/SUM22
- U29 pad 9: /BUS7 -> /ALU/SUM23
- U3 pad 14: /47KHZ_CLK -> /Clock/47_KHZ_CLK
- U3 pad 6: (no net) -> Net-(U3-Pad6)
- U31 pad 1: /MLU_SEL2 -> VCC
- U31 pad 10: /A2 -> GND
- U31 pad 11: /A1 -> /BUS23
- U31 pad 12: /A0 -> /BUS22
- U31 pad 13: /BUS0 -> /BUS21
- U31 pad 14: /BUS1 -> /BUS20
- U31 pad 15: /BUS2 -> /BUS19
- U31 pad 16: GND -> /BUS18
- U31 pad 17: /BUS3 -> /BUS17
- U31 pad 18: /BUS4 -> /BUS16
- U31 pad 19: /BUS5 -> /~NAND_OUT_NCLK
- U31 pad 2: /MLU_SEL0 -> /ALU/NAND16
- U31 pad 20: /BUS6 -> VCC
- U31 pad 3: /B7 -> /ALU/NAND17
- U31 pad 4: /B4 -> /ALU/NAND18
- U31 pad 5: /A7 -> /ALU/NAND19
- U31 pad 6: /A6 -> /ALU/NAND20
- U31 pad 7: /A5 -> /ALU/NAND21
- U31 pad 8: /A4 -> /ALU/NAND22
- U31 pad 9: /A3 -> /ALU/NAND23
- U32 pad 1: /~S2_OUT_NCLK -> /ALU/A8
- U32 pad 10: GND -> /ALU/B10
- U32 pad 11: /S2_IN_CLK -> /ALU/NAND11
- U32 pad 12: /BUS7 -> /ALU/A11
- U32 pad 13: /BUS6 -> /ALU/B11
- U32 pad 14: /BUS5 -> VCC
- U32 pad 2: /BUS0 -> /ALU/B8
- U32 pad 3: /BUS1 -> /ALU/NAND8
- U32 pad 4: /BUS2 -> /ALU/A9
- U32 pad 5: /BUS3 -> /ALU/B9
- U32 pad 6: /BUS4 -> /ALU/NAND9
- U32 pad 7: /BUS5 -> GND
- U32 pad 8: /BUS6 -> /ALU/NAND10
- U32 pad 9: /BUS7 -> /ALU/A10
- U33 pad 11: (no net) -> Net-(U33-Pad11)
- U33 pad 8: (no net) -> Net-(U33-Pad8)
- U34 pad 1: /~PC0_OUT_NCLK -> /ALU/SUM25
- U34 pad 10: GND -> /ALU/SUM27
- U34 pad 11: /PC0_IN_CLK -> /ALU/B27
- U34 pad 12: /BUS7 -> /ALU/A27
- U34 pad 13: /BUS6 -> /ALU/SUM26
- U34 pad 14: /BUS5 -> /ALU/A26
- U34 pad 15: /BUS4 -> /ALU/B26
- U34 pad 16: /BUS3 -> VCC
- U34 pad 2: /BUS0 -> /ALU/B25
- U34 pad 3: /BUS1 -> /ALU/A25
- U34 pad 4: /BUS2 -> /ALU/SUM24
- U34 pad 5: /BUS3 -> /ALU/A24
- U34 pad 6: /BUS4 -> /ALU/B24
- U34 pad 7: /BUS5 -> /ALU/CARRY5
- U34 pad 8: /BUS6 -> GND
- U34 pad 9: /BUS7 -> /ALU/CARRY6
- U35 pad 2: (no net) -> Net-(U35-Pad2)
- U35 pad 3: (no net) -> Net-(U35-Pad3)
- U35 pad 6: (no net) -> Net-(U35-Pad6)
- U36 pad 10: /INT5_IN_CLK -> /Control Logic/IN decoder/O29
- U36 pad 11: /INT4_IN_CLK -> /Control Logic/IN decoder/O28
- U36 pad 12: /INT3_IN_CLK -> /Control Logic/IN decoder/O27
- U36 pad 13: /INT2_IN_CLK -> /Control Logic/IN decoder/O26
- U36 pad 14: /INT1_IN_CLK -> /Control Logic/IN decoder/O25
- U36 pad 15: /INT0_IN_CLK -> /Control Logic/IN decoder/O24
- U36 pad 7: /INT7_IN_CLK -> /Control Logic/IN decoder/O31
- U36 pad 9: /INT6_IN_CLK -> /Control Logic/IN decoder/O30
- U37 pad 10: (no net) -> Net-(U37-Pad10)
- U37 pad 11: /~UNSET_INT_ENABLE_ASYNC -> Net-(U37-Pad11)
- U37 pad 12: /~SET_INT_ENABLE_ASYNC -> /CARRY_IN
- U37 pad 15: (no net) -> Net-(U37-Pad15)
- U37 pad 7: (no net) -> Net-(U37-Pad7)
- U37 pad 9: (no net) -> Net-(U37-Pad9)
- U38 pad 1: /~UNSET_INT_ENABLE_ASYNC -> /Control Logic/~BUS2_OUT_NCLK
- U38 pad 10: VCC -> GND
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
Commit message: Layout progress.
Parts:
- added C103: 0.1uF, Capacitor_THT:C_Disc_D6.0mm_W2.5mm_P5.00mm, F.Cu at (-157.5, 183.0)
- added RN2: 100K, Resistor_THT:R_Array_SIP9, F.Cu at (47.0, 105.5)
- added RN3: 100K, Resistor_THT:R_Array_SIP9, F.Cu at (76.5, 105.5)
- added RN4: 100K, Resistor_THT:R_Array_SIP9, F.Cu at (107.0, 105.5)
- added RN5: 100K, Resistor_THT:R_Array_SIP9, F.Cu at (137.0, 105.5)
- added U86: 74HC245, Package_DIP:DIP-20_W7.62mm_Socket, F.Cu at (-154.0, 189.5)
- moved C59 618.0 mm to (-173.0, 294.5), turned to 90 degrees
- moved C60 617.0 mm to (-183.0, 224.0), turned to 90 degrees
- moved C52 611.0 mm to (-135.5, 287.0)
- moved C53 608.6 mm to (-135.5, 301.5)
- moved C57 598.6 mm to (-173.0, 268.0), turned to 90 degrees
- moved U45 598.3 mm to (-136.0, 312.5), turned to 90 degrees
- moved U51 593.6 mm to (-179.5, 219.5)
- moved U52 592.7 mm to (-169.5, 289.5)
- moved C58 586.7 mm to (-183.0, 197.5), turned to 90 degrees
- moved U44 571.3 mm to (-136.0, 298.0), turned to 90 degrees
- moved U48 559.9 mm to (-179.5, 193.0)
- moved C50 547.9 mm to (-74.0, 264.5), turned to 180 degrees
- moved U47 543.3 mm to (-58.5, 313.5), turned to 90 degrees
- moved C49 542.6 mm to (-69.5, 276.5), turned to 270 degrees
- moved C61 541.2 mm to (-113.0, 224.5), turned to 90 degrees
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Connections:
- J1 pad 2: Net-(J1-Pad2) -> (no net)
- J1 pad 3: Net-(J1-Pad3) -> (no net)
- J1 pad 4: Net-(J1-Pad4) -> (no net)
- J3 pad 3: Net-(J3-Pad3) -> (no net)
- J4 pad 22: Net-(J4-Pad22) -> (no net)
- J4 pad 24: Net-(J4-Pad24) -> (no net)
- J4 pad 26: Net-(J4-Pad26) -> (no net)
- J4 pad 28: Net-(J4-Pad28) -> (no net)
- J4 pad 30: Net-(J4-Pad30) -> (no net)
- J4 pad 32: Net-(J4-Pad32) -> (no net)
- J4 pad 34: Net-(J4-Pad34) -> (no net)
- J4 pad 36: Net-(J4-Pad36) -> (no net)
- J4 pad 38: Net-(J4-Pad38) -> (no net)
- J4 pad 40: Net-(J4-Pad40) -> (no net)
- U114 pad 12: Net-(U114-Pad12) -> (no net)
- U114 pad 4: Net-(U114-Pad4) -> (no net)
- U114 pad 6: Net-(U114-Pad6) -> (no net)
- U15 pad 16: Net-(U15-Pad16) -> (no net)
- U15 pad 19: Net-(U15-Pad19) -> (no net)
- U17 pad 15: /Control Logic/IN decoder/O0 -> (no net)
- U2 pad 8: Net-(U2-Pad8) -> (no net)
- U20 pad 10: /Control Logic/IN decoder/O21 -> (no net)
- U20 pad 11: /Control Logic/IN decoder/O20 -> (no net)
- U20 pad 12: /Control Logic/IN decoder/O19 -> (no net)
- U20 pad 7: /Control Logic/IN decoder/O23 -> (no net)
- U20 pad 9: /Control Logic/IN decoder/O22 -> (no net)
- U3 pad 6: Net-(U3-Pad6) -> (no net)
- U33 pad 11: Net-(U33-Pad11) -> (no net)
- U33 pad 8: Net-(U33-Pad8) -> (no net)
- U35 pad 2: Net-(U35-Pad2) -> (no net)
- U35 pad 3: Net-(U35-Pad3) -> (no net)
- U35 pad 6: Net-(U35-Pad6) -> (no net)
- U36 pad 10: /Control Logic/IN decoder/O29 -> (no net)
- U36 pad 11: /Control Logic/IN decoder/O28 -> (no net)
- U36 pad 12: /Control Logic/IN decoder/O27 -> (no net)
- U36 pad 13: /Control Logic/IN decoder/O26 -> (no net)
- U36 pad 14: /Control Logic/IN decoder/O25 -> (no net)
- U36 pad 15: /Control Logic/IN decoder/O24 -> (no net)
- U36 pad 7: /Control Logic/IN decoder/O31 -> (no net)
- U36 pad 9: /Control Logic/IN decoder/O30 -> (no net)
- U37 pad 10: Net-(U37-Pad10) -> (no net)
- U37 pad 11: Net-(U37-Pad11) -> (no net)
- U37 pad 15: Net-(U37-Pad15) -> (no net)
- U37 pad 7: Net-(U37-Pad7) -> (no net)
- U37 pad 9: Net-(U37-Pad9) -> (no net)
- U39 pad 5: Net-(U39-Pad5) -> (no net)
- U39 pad 6: Net-(U39-Pad6) -> (no net)
- U39 pad 7: Net-(U39-Pad7) -> (no net)
- U39 pad 9: Net-(U39-Pad9) -> (no net)
- U40 pad 9: /ALU/CARRY_OUT -> (no net)
- U5 pad 10: Net-(U5-Pad10) -> (no net)
- U5 pad 8: /ALU/ZERO_OUT -> (no net)
- U6 pad 3: /Clock/750KHZ_CLK -> (no net)
- U6 pad 4: /Clock/375KHZ_CLK -> (no net)
- U6 pad 6: /Clock/94_KHZ_CLK -> (no net)
- U6 pad 9: Net-(U6-Pad9) -> (no net)
- U89 pad 12: Net-(U89-Pad12) -> (no net)
- U89 pad 13: Net-(U89-Pad13) -> (no net)
- U89 pad 14: Net-(U89-Pad14) -> (no net)
- U95 pad 1: /Control Logic/OUT plane decoder/O0 -> (no net)
- U95 pad 15: /Control Logic/~BUS0_OUT_NCLK -> (no net)
- U95 pad 16: /Control Logic/~BUS1_OUT_NCLK -> /Control Logic/~BUS0_OUT_NCLK
- U95 pad 17: /Control Logic/~BUS2_OUT_NCLK -> /Control Logic/~BUS1_OUT_NCLK
- U96 pad 1: /Control Logic/~BUS3_OUT_NCLK -> /Control Logic/~BUS2_OUT_NCLK
- U96 pad 10: /Control Logic/OUT plane decoder/O25 -> (no net)
- U96 pad 11: /Control Logic/OUT plane decoder/O26 -> (no net)
- U96 pad 13: /Control Logic/OUT plane decoder/O27 -> (no net)
- U96 pad 14: /Control Logic/OUT plane decoder/O28 -> (no net)
- U96 pad 15: /Control Logic/OUT plane decoder/O29 -> (no net)
- U96 pad 16: /Control Logic/OUT plane decoder/O30 -> (no net)
- U96 pad 17: /Control Logic/OUT plane decoder/O31 -> (no net)
- U96 pad 2: /Control Logic/OUT plane decoder/O17 -> /Control Logic/~BUS3_OUT_NCLK
- U96 pad 3: /Control Logic/OUT plane decoder/O18 -> (no net)
- U96 pad 4: /Control Logic/OUT plane decoder/O19 -> (no net)
- U96 pad 5: /Control Logic/OUT plane decoder/O20 -> (no net)
- U96 pad 6: /Control Logic/OUT plane decoder/O21 -> (no net)
- U96 pad 7: /Control Logic/OUT plane decoder/O22 -> (no net)
- U96 pad 8: /Control Logic/OUT plane decoder/O23 -> (no net)
- U96 pad 9: /Control Logic/OUT plane decoder/O24 -> (no net)
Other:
- board text added: "ALU NAND"
- board text added: "ALU NAND Buf"
- board text added: "ALU SUM Buf"
- board text added: "ALU Status Buf"
- board text added: "Adders"
- board text added: "Boot EEPROM"
- board text added: "Bus Out Latch"
- board text added: "OR logic for ZERO"
- board text added: "OUT Plane Latch"
- board text added: "Reg A"
- board text added: "Reg ADDR"
- board text added: "Reg ALU0"
- board text added: "Reg ALU1"
- board text added: "Reg B"
- board text added: "Reg M"
- board text added: "Reg PC"
- board text added: "Reg Page"
- board text added: "Reg SP"
- board text added: "Reg Status"
- board text added: "SRAM"
- board text removed: "A"
- board text removed: "B"
- board text removed: "Display Module"
- board text removed: "Flag Logic"
- board text removed: "In Plane Decoder"
- board text removed: "M0"
- board text removed: "M1"
- board text removed: "M2"
- board text removed: "MLU"
- board text removed: "MMU"
- board text removed: "MMU Fault Logic"
- board text removed: "MMU Protection"
- board text removed: "MMU0"
- board text removed: "MMU1"
- board text removed: "MMU2"
- board text removed: "Program Counter"
- board text removed: "SRAM Select"
- board text removed: "Stack Pointer"
- board text removed: "Status"
- board text removed: "Status Reg Buf"
- board text removed: "Task"
